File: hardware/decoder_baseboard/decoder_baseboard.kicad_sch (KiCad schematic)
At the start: 9 parts, among them J1 Conn_02x32_Counter_Clockwise, J2 USB_C_Receptacle_USB2.0, U1 SN74AVC8T245PW, U5 PicoW

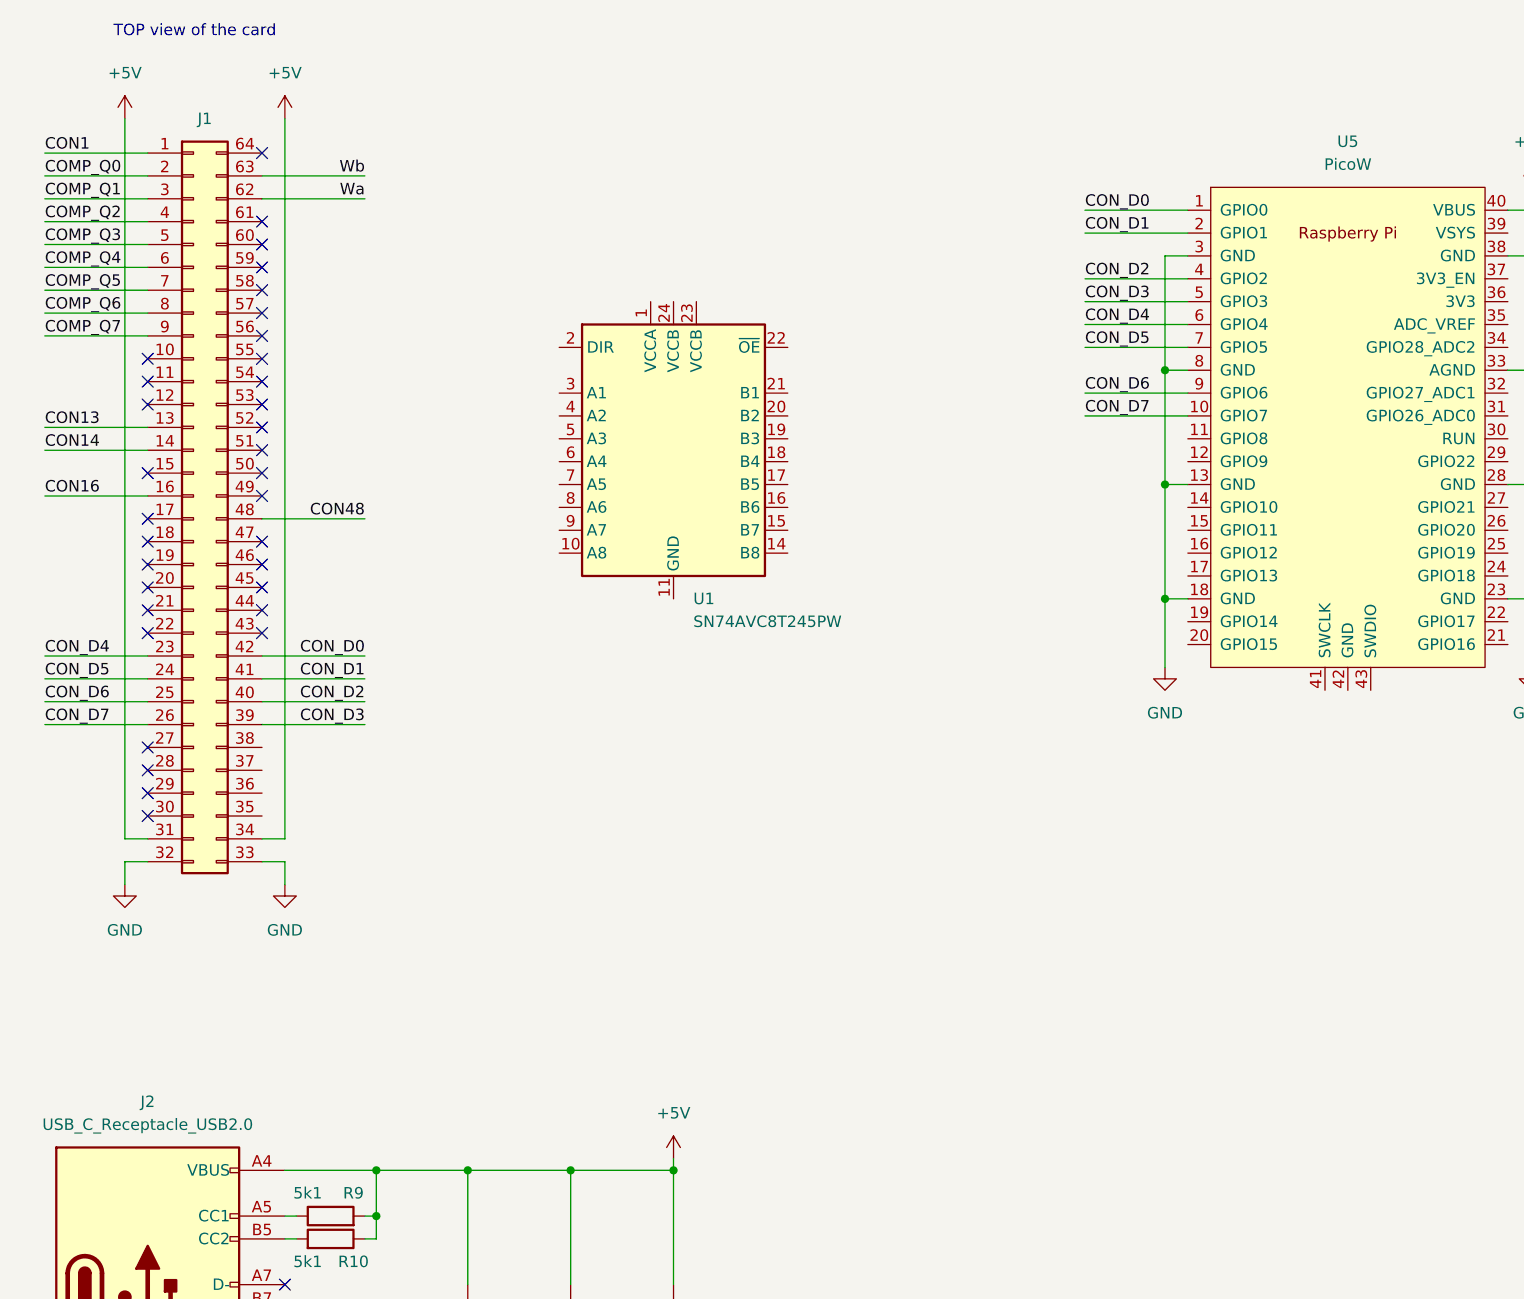
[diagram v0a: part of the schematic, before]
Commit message: Added PICO footprint and USB
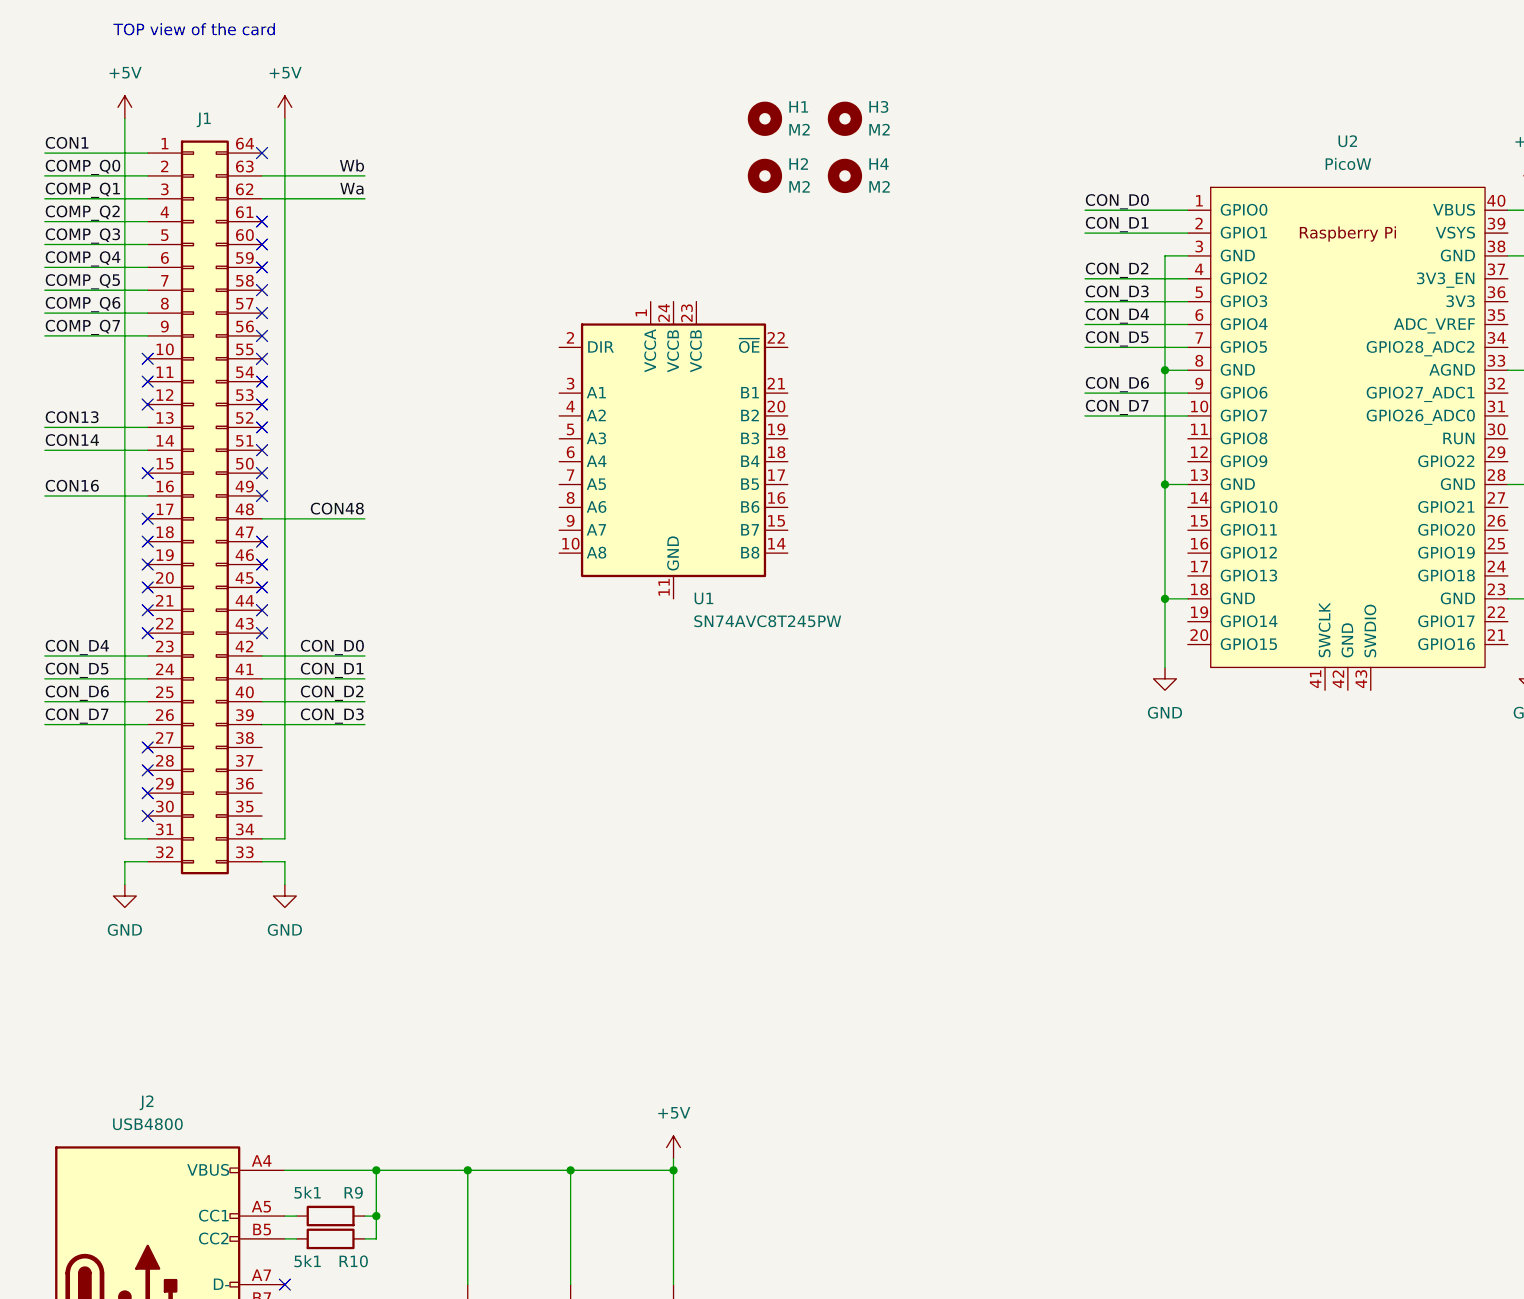
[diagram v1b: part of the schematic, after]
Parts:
- removed U5: PicoW, RPi_PicoW:RPi_Pico_SMD_TH, symbol RPi_Pico:PicoW
- added H1, H2, H3, H4: M2, MountingHole:MountingHole_2.2mm_M2_DIN965_Pad, symbol Mechanical:MountingHole
- added U2: PicoW, RPi_PicoW:RPi_Pico_SMD_TH, symbol RPi_Pico:PicoW
- J2: value USB_C_Receptacle_USB2.0 -> USB4800; footprint Connector_USB:USB_C_Receptacle_XKB_U262-16XN-4BVC11 -> Connector_USB:USB_C_Receptacle_GCT_USB4105-xx-A_16P_TopMnt_Horizontal
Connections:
- net +5V: now also U2.40 (VBUS)
- net CON_D0: now also U2.1 (GPIO0)
- net CON_D1: now also U2.2 (GPIO1)
- net CON_D2: now also U2.4 (GPIO2)
- net CON_D3: now also U2.5 (GPIO3)
- net CON_D4: now also U2.6 (GPIO4)
- net CON_D5: now also U2.7 (GPIO5)
- net CON_D6: now also U2.9 (GPIO6)
- net CON_D7: now also U2.10 (GPIO7)
- net GND: now also U2.13 (GND), U2.18 (GND), U2.23 (GND), U2.28 (GND), U2.3 (GND), U2.33 (AGND), U2.38 (GND), U2.8 (GND)

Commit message: Some routing done
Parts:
- removed D1: PESD5V0L1UA, symbol Device:D_Zener
- removed J1: Conn_02x32_Counter_Clockwise, symbol Connector_Generic:Conn_02x32_Counter_Clockwise
- removed J2: USB4800, Connector_USB:USB_C_Receptacle_GCT_USB4105-xx-A_16P_TopMnt_Horizontal, symbol Connector:USB_C_Receptacle_USB2.0
- removed U1: SN74AVC8T245PW, Package_SO:TSSOP-24_4.4x7.8mm_P0.65mm, symbol Logic_LevelTranslator:SN74AVC8T245PW
- added C10, C2, C4, C5, C6, C9: 100n, Capacitor_SMD:C_0603_1608Metric, symbol Device:C
- added C11, C7, C8: 10u, Capacitor_SMD:C_0603_1608Metric, symbol Device:C
- added D1: LED FILAMENT, decoder:Con_01x02_2.54_SMD, symbol Device:LED
- added D2: BAV99, Package_TO_SOT_SMD:SOT-23, symbol Diode:BAV99
- added J1: Conn_02x32_Odd_Even, Connector_PinSocket_2.54mm:PinSocket_2x32_P2.54mm_Vertical_SMD, symbol Connector_Generic:Conn_02x32_Odd_Even
- added J3: USB4800, Connector_USB:USB_C_Receptacle_XKB_U262-16XN-4BVC11, symbol Connector:USB_C_Receptacle_USB2.0
- added JP1, JP2, JP3, JP4, JP5, JP6, JP7, JP8: SolderJumper_3_Bridged12, Jumper:SolderJumper-3_P1.3mm_Bridged2Bar12_Pad1.0x1.5mm, symbol Jumper:SolderJumper_3_Bridged12
- added LS1: PKMCS0909E, Buzzer_Beeper:Buzzer_Murata_PKMCS0909E, symbol Device:Speaker
- added Q1, Q2: BSS138, Package_TO_SOT_SMD:SOT-23, symbol Transistor_FET:BSS138
- added R1, R2: 5k1, Resistor_SMD:R_0603_1608Metric, symbol Device:R
- added R3: 22k, Resistor_SMD:R_0603_1608Metric, symbol Device:R
- added R4: 33k, Resistor_SMD:R_0603_1608Metric, symbol Device:R
- added R5, R7, R8: 10k, Resistor_SMD:R_0603_1608Metric, symbol Device:R
- added R6: 33, Resistor_SMD:R_0603_1608Metric, symbol Device:R
- added U1: SN74LXC8T245, Package_SO:TSSOP-24_4.4x7.8mm_P0.65mm, symbol Logic_LevelTranslator:SN74LVC8T245
- added U3: USBLC6-2SC6, Package_TO_SOT_SMD:SOT-23-6, symbol Power_Protection:USBLC6-2SC6
- added U4: LIS2DW12, Package_LGA:LGA-12_2x2mm_P0.5mm, symbol decoder:LIS2DW12
- added U6: SN74HCS244, Package_SO:TSSOP-20_4.4x6.5mm_P0.65mm, symbol 74xx:74AHC244
- C1: value 1u -> 10u
- C3: value 10u -> 100n
- R10: value 5k1 -> 1k
- R9: value 5k1 -> 100
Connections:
- net +5V: now also C1.1, R9.1, U2.39 (VSYS), C11.1, C5.1, C6.1, C7.1, C8.1, C9.1, J1.61 (Pin_61), J1.62 (Pin_62), J3.A4 (VBUS), J3.A9 (VBUS), J3.B4 (VBUS), J3.B9 (VBUS), JP1.2 (C), JP2.2 (C), JP3.2 (C), JP4.2 (C), JP5.2 (C), JP6.2 (C), JP7.2 (C), JP8.2 (C), R1.2, R2.1, R6.1, U1.23 (V_{CCB}), U1.24 (V_{CCB}), U3.5 (VBUS), U6.20 (VCC); no longer C1.2, R10.1, R9.2
- net GND: now also C1.2, U2.45 (GND), C10.2, C11.2, C2.2, C4.2, C5.2, C6.2, C7.2, C8.2, C9.2, D2.1 (K), J1.1 (Pin_1), J1.2 (Pin_2), J1.63 (Pin_63), J1.64 (Pin_64), J3.A1 (GND), J3.A12 (GND), J3.B1 (GND), J3.B12 (GND), J3.S1 (SHIELD), JP1.3 (B), JP2.3 (B), JP3.3 (B), JP4.3 (B), JP5.3 (B), JP6.3 (B), JP7.3 (B), JP8.3 (B), Q1.2 (S), Q2.2 (S), R4.2, R7.1, R8.1, U1.11 (GND), U1.12 (GND), U1.13 (GND), U3.2 (GND), U4.6 (GND), U4.7 (RES), U4.8 (GND), U6.10 (GND); no longer C1.1
- net at R10.2: now also LS1.2, Q2.3 (D)
- net +3V3: now reaches U2.36 (3V3)
- net +3V3: now also C10.1, C4.1, D2.2 (A), R5.1, U1.1 (V_{CCA}), U4.10 (Vdd_IO), U4.9 (Vdd)
- net CON_D0: no longer names the net of U2.1 (GPIO0)
- net CON_D1: no longer names the net of U2.2 (GPIO1)
- net CON_D2: no longer names the net of U2.4 (GPIO2)
- net CON_D3: no longer names the net of U2.5 (GPIO3)
- net CON_D4: no longer names the net of U2.6 (GPIO4)
- net CON_D5: no longer names the net of U2.7 (GPIO5)
- net CON_D6: no longer names the net of U2.9 (GPIO6)
- net CON_D7: no longer names the net of U2.10 (GPIO7)
- new net: J3.A5 (CC1), R1.1
- new net: J3.A6 (D+), J3.B6 (D+), U3.3 (I/O2)
- new net: J3.A7 (D-), J3.B7 (D-), U3.1 (I/O1)
- new net: J3.B5 (CC2), R2.2
- new net: LS1.1, R10.1, R9.2
- new net: D1.1 (K), Q1.3 (D)
- new net: D1.2 (A), R6.2
- new net: R5.2, U1.22 (~{OE})
- new net +12V: J1.60 (Pin_60)
- new net ACCEL_INT1: U4.12 (INT1)
- new net ACCEL_INT2: U4.11 (INT2)
- new net ACCEL_SCL: U4.1 (SCL/SPC)
- new net ACCEL_SDA: U4.4 (SDA/SDI)
- new net ACCEL_~{CS}: U4.2 (~{CS})
- new net BACKLIGHT_PWM: Q1.1 (G), R7.2
- new net BUZZER_PWM: Q2.1 (G), R8.2
- new net CARD_A0: J1.3 (Pin_3), JP1.1 (A)
- new net CARD_A1: J1.5 (Pin_5), JP2.1 (A)
- new net CARD_A2: J1.7 (Pin_7), JP3.1 (A)
- new net CARD_A3: J1.9 (Pin_9), JP4.1 (A)
- new net CARD_A4: J1.11 (Pin_11), JP5.1 (A)
- new net CARD_A5: J1.13 (Pin_13), JP6.1 (A)
- new net CARD_A6: J1.15 (Pin_15), JP7.1 (A)
- new net CARD_A7: J1.17 (Pin_17), JP8.1 (A)
- new net FIFO_EXT_A0: J1.6 (Pin_6), U6.3 (2Y0)
- new net FIFO_EXT_A1: J1.4 (Pin_4), U6.12 (1Y3)
- new net FIFO_EXT_D0: J1.46 (Pin_46), U1.14 (B8)
- new net FIFO_EXT_D1: J1.48 (Pin_48), U1.16 (B6)
- new net FIFO_EXT_D2: J1.50 (Pin_50), U1.18 (B4)
- new net FIFO_EXT_D3: J1.52 (Pin_52), U1.20 (B2)
- new net FIFO_EXT_D4: J1.45 (Pin_45), U1.15 (B7)
- new net FIFO_EXT_D5: J1.47 (Pin_47), U1.17 (B5)
- new net FIFO_EXT_D6: J1.49 (Pin_49), U1.19 (B3)
- new net FIFO_EXT_D7: J1.51 (Pin_51), U1.21 (B1)
- new net FIFO_EXT_EN: J1.25 (Pin_25), U6.18 (1Y0)
- new net FIFO_EXT_R/~{W}: J1.34 (Pin_34), U6.16 (1Y1)
- new net USB_D+: U2.44 (DP), U3.4 (I/O2)
- new net USB_D-: U2.46 (DM), U3.6 (I/O1)
- new net VBUS: R3.1
- new net VBUS_SENSE: C2.1, D2.3 (K), R3.2, R4.1
- new net ~{RESET}: J1.27 (Pin_27), U6.14 (1Y2)
- no-connect marks 39 -> 42
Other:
- note added: "I2C_ADD = 0x19"
- note added: "LED Filament Max 100mA @ 3V"
- note removed: "TOP view of the card"
- moved on the sheet: H1, H2, H3, H4
